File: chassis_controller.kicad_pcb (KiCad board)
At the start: 2 copper layers, 99.3 x 72.7 mm, 128 parts, among them J1 Screw_Terminal_01x02, J10 Conn_01x04_Pin, J11 Conn_02x03_Odd_Even, J12 Conn_01x04_Pin, J13 Conn_01x04_Pin, J14 Conn_01x04_Pin, J15 Conn_01x04_Pin, J16 Conn_01x04_Pin, J17 Conn_01x04_Pin, J18 Conn_01x03_Pin, J19 Conn_01x03_Pin, J2 Conn_01x04_Pin, J20 Conn_01x03_Pin, J21 Conn_01x04_Pin, J22 Conn_01x03_Pin, J23 Conn_01x03_Pin, J24 Conn_01x03_Pin, J25 Conn_01x03_Pin, J3 Conn_01x02_Pin, J4 Conn_01x02_Pin, J5 Conn_01x03_Pin, J6 Conn_01x03_Pin, J7 Conn_01x04_Pin, J8 Conn_01x04_Pin, J9 Conn_01x04_Pin, Q2 HSBA100P04, Q4 HSBA100P04, U1 AP64500SP-13, U2 AMS1117-3.3, U3 DSHP04TSGER, U4 STM32F407VGT6TR, U5 PCA9685PW,118, U6 PCA9685PW,118, U7 MPU-6050, U8 SN65HVD230DR, X1 X32258MOB4SI

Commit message: Add improvements to project
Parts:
- removed J11: Conn_02x03_Odd_Even, Connector_IDC:IDC-Header_2x03_P2.54mm_Vertical
- added C46: 1000uF, Capacitor_THT:CP_Radial_D10.0mm_P5.00mm, F.Cu at (153.0, 115.8)
- added C47: 1000uF, Capacitor_THT:CP_Radial_D10.0mm_P5.00mm, F.Cu at (164.0, 115.8)
- added J26: Conn_01x06_Pin, Connector_JST:JST_PH_B6B-PH-K_1x06_P2.00mm_Vertical, F.Cu at (128.8, 66.6)
- added Q1: NMOS, Package_TO_SOT_SMD:SOT-23, B.Cu at (155.7, 129.0)
- added R16: 47k, Resistor_SMD:R_0805_2012Metric, B.Cu at (154.7, 122.8)
- BUZZER1, D3, U3: moved to F.Cu
- R1, R11, R4, R7: moved to B.Cu
- R19: value 10 -> 10k
- moved JP1 30.5 mm to (135.9, 121.7)
- moved J25 30.5 mm to (131.8, 127.4)
- moved R35 30.5 mm to (133.5, 121.7)
- moved R34 21.9 mm to (140.7, 112.5)
- moved U8 21.9 mm to (142.4, 116.5)
- moved R18 17.9 mm to (159.4, 130.0), turned to 180 degrees
- moved R19 15.8 mm to (154.7, 126.0), turned to 0 degrees
- moved C38 15.1 mm to (127.7, 80.8)
- moved D1 15.0 mm to (172.6, 129.1)
- moved D4 15.0 mm to (170.4, 129.1)
- moved D5 15.0 mm to (168.0, 129.1)
- moved D6 15.0 mm to (165.6, 129.0)
- moved R1 15.0 mm to (172.6, 125.6)
- moved R11 15.0 mm to (165.8, 125.5)
- moved R4 15.0 mm to (170.4, 125.5)
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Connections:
- Q4 pad 4: Net-(Q4-G) -> Net-(Q1-D)
- R18 pad 2: Net-(Q4-G) -> Net-(Q1-D)
- R19 pad 1: /SERVO_PWR -> Net-(Q1-G)
- R19 pad 2: Net-(Q4-G) -> GND
- U4 pad 25: /MOTOR3_PWM -> unconnected-(U4-PA2-Pad25)
- U4 pad 26: /MOTOR4_PWM -> unconnected-(U4-PA3-Pad26)
- U4 pad 61: /MOTOR1_PWM -> unconnected-(U4-PD14-Pad61)
- U4 pad 62: /MOTOR2_PWM -> unconnected-(U4-PD15-Pad62)
- U5 pad 10: /MOTOR1_FWD -> /MOTOR1_PWM
- U5 pad 11: /MOTOR1_RVR -> /MOTOR1_FWD
- U5 pad 12: /MOTOR2_FWD -> /MOTOR1_RVR
- U5 pad 13: /MOTOR2_RVR -> /MOTOR2_PWM
- U5 pad 15: /MOTOR3_FWD -> /MOTOR2_FWD
- U5 pad 16: /MOTOR3_RVR -> /MOTOR2_RVR
- U5 pad 17: /MOTOR4_FWD -> /MOTOR3_PWM
- U5 pad 18: /MOTOR4_RVR -> /MOTOR3_FWD
- U5 pad 19: unconnected-(U5-LED12-Pad19) -> /MOTOR3_RVR
- U5 pad 20: unconnected-(U5-LED13-Pad20) -> /MOTOR4_PWM
- U5 pad 21: unconnected-(U5-LED14-Pad21) -> /MOTOR4_FWD
- U5 pad 22: unconnected-(U5-LED15-Pad22) -> /MOTOR4_RVR
- X1 pad 2: /OSC_IN -> GND
- X1 pad 3: GND -> /OSC_IN

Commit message: Update project
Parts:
- removed C39: 10nF, Capacitor_SMD:C_0805_2012Metric
- added C48: 1000uF, Capacitor_THT:CP_Radial_D10.0mm_P5.00mm, F.Cu at (150.0, 117.5)
- added G***: LOGO, kpi-rover:kpi-rover-logo, F.Cu at (121.3, 108.7)
- added Q3: NMOS, Package_TO_SOT_SMD:SOT-23, B.Cu at (169.6, 71.1)
- added R36: 4.7k, Resistor_SMD:R_0805_2012Metric, B.Cu at (173.6, 70.2)
- added R37: 4.7k, Resistor_SMD:R_0805_2012Metric, B.Cu at (182.6, 125.8)
- added R38: 0, Resistor_SMD:R_0805_2012Metric, B.Cu at (191.8, 70.3)
- added R39: 0, Resistor_SMD:R_0805_2012Metric, B.Cu at (182.6, 128.2)
- added R40: 0, Resistor_SMD:R_0805_2012Metric, B.Cu at (141.9, 118.4)
- added R41: 330, Resistor_SMD:R_0805_2012Metric, B.Cu at (173.6, 62.0)
- added R42: 1k, Resistor_SMD:R_0805_2012Metric, B.Cu at (155.7, 69.0)
- added R43: 1k, Resistor_SMD:R_0805_2012Metric, B.Cu at (141.0, 69.0)
- added R44: 2k, Resistor_SMD:R_0805_2012Metric, B.Cu at (155.7, 72.0)
- added R45: 2k, Resistor_SMD:R_0805_2012Metric, B.Cu at (141.0, 72.0)
- added R46: 0, Resistor_SMD:R_0805_2012Metric, B.Cu at (154.8, 75.7)
- added R47: 0, Resistor_SMD:R_0805_2012Metric, B.Cu at (123.1, 88.3)
- added R48: 0, Resistor_SMD:R_0805_2012Metric, B.Cu at (170.1, 130.5)
- added R49: 0, Resistor_SMD:R_0805_2012Metric, B.Cu at (127.9, 84.6)
- added R50: 0, Resistor_SMD:R_0805_2012Metric, B.Cu at (194.7, 65.0)
- added R51: 0, Resistor_SMD:R_0805_2012Metric, B.Cu at (170.4, 96.4)
- added R52: 0, Resistor_SMD:R_0805_2012Metric, B.Cu at (140.3, 87.0)
- C46: value 1000uF -> 100nF; footprint Capacitor_THT:CP_Radial_D10.0mm_P5.00mm -> Capacitor_SMD:C_0805_2012Metric; moved to B.Cu
- J3: value Conn_01x02_Pin -> Screw_Terminal_01x02; footprint Connector_JST:JST_PH_B2B-PH-K_1x02_P2.00mm_Vertical -> DB127V-5.08-2P-GN-S:CONN-TH_2P-P5.08
- moved C1 57.1 mm to (153.8, 79.2)
- moved C46 46.1 mm to (131.3, 75.2), turned to -90 degrees
- moved J22 16.4 mm to (192.4, 105.2), turned to -90 degrees
- moved J24 13.9 mm to (199.4, 105.2), turned to -90 degrees
- moved J26 13.8 mm to (115.2, 64.5), turned to 0 degrees
- moved C26 13.7 mm to (129.6, 65.4)
- moved C27 13.6 mm to (129.6, 67.6)
- moved D6 13.5 mm to (179.0, 130.4)
- moved C10 13.3 mm to (178.3, 87.4), turned to 90 degrees
- moved R11 13.2 mm to (179.0, 126.4)
- moved C12 13.2 mm to (185.3, 87.4), turned to 90 degrees
- moved C19 13.2 mm to (199.5, 87.4), turned to 90 degrees
- moved C17 13.1 mm to (192.4, 87.4), turned to 90 degrees
- moved C13 12.8 mm to (183.2, 87.4), turned to 90 degrees
- moved C11 12.8 mm to (176.2, 87.4), turned to 90 degrees
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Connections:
- BUZZER1 pad 1: +5V -> Net-(BUZZER1-Pad1)
- BUZZER1 pad 2: /BUZZER_OUT -> Net-(Q3-D)
- C15 pad 1: +5V -> Net-(U2-VIN)
- C36 pad 1: +5V -> Net-(U5-VDD)
- C37 pad 1: +5V -> Net-(U6-VDD)
- C43 pad 1: +3.3V -> Net-(U7-VDD)
- C46 pad 1: /SERVO_5V -> GND
- C46 pad 2: GND -> Net-(U7-VDD)
- C47 pad 1: /SERVO_5V -> +5V
- J14 pad 4: /USS1_ECHO -> Net-(J14-Pin_4)
- J15 pad 4: /USS2_ECHO -> Net-(J15-Pin_4)
- R1 pad 2: +5V -> Net-(R1-Pad2)
- R11 pad 2: +5V -> Net-(R1-Pad2)
- R22 pad 1: +3.3V -> Net-(R22-Pad1)
- R23 pad 1: +3.3V -> Net-(R22-Pad1)
- R24 pad 1: +3.3V -> Net-(R22-Pad1)
- R25 pad 1: +3.3V -> Net-(R22-Pad1)
- R28 pad 1: +5V -> Net-(R28-Pad1)
- R29 pad 1: +5V -> Net-(R28-Pad1)
- R30 pad 1: +3.3V -> Net-(U7-VDD)
- R31 pad 1: +3.3V -> Net-(U7-VDD)
- R4 pad 2: +5V -> Net-(R1-Pad2)
- R7 pad 2: +5V -> Net-(R1-Pad2)
- U2 pad 3: +5V -> Net-(U2-VIN)
- U5 pad 1: GND -> Net-(U5-A0)
- U5 pad 28: +5V -> Net-(U5-VDD)
- U6 pad 2: GND -> Net-(U6-A1)
- U6 pad 28: +5V -> Net-(U6-VDD)
- U7 pad 13: +3.3V -> Net-(U7-VDD)
- U7 pad 8: +3.3V -> Net-(U7-VDD)
- U7 pad 9: unconnected-(U7-AD0-Pad9) -> GND
- U8 pad 3: +3.3V -> Net-(U8-VCC)
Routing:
- net +3.3V: track 0.00 -> 302.1 mm, vias 0 -> 13
- net +5V: track 0.00 -> 241.8 mm, vias 0 -> 136
- net /SERVO_5V: track 0.00 -> 135.8 mm, vias 0 -> 18
- net /PCA_I2C_SCL: track 0.00 -> 103.3 mm, vias 0 -> 4
- net /PCA_I2C_SDA: track 0.00 -> 102.7 mm, vias 0 -> 4
- net /POWER_SUPPLY_ADC: track 0.00 -> 69.3 mm, vias 0 -> 2
- net /SWCLK: track 0.00 -> 53.3 mm, vias 0 -> 1
- net /ENC4_B: track 0.00 -> 52.7 mm, vias 0 -> 1
- net /ENC4_A: track 0.00 -> 52.7 mm, vias 0 -> 1
- net /SWDIO: track 0.00 -> 51.2 mm, vias 0 -> 1
- net /STATUS_LED_4: track 0.00 -> 47.1 mm, vias 0 -> 1
- net /ENC2_A: track 0.00 -> 44.4 mm, vias 0 -> 1
- net /ENC2_B: track 0.00 -> 44.2 mm, vias 0 -> 1
- net /NRST: track 0.00 -> 44.2 mm
- net /STATUS_LED_3: track 0.00 -> 43.9 mm, vias 0 -> 1
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- added copper zone on B.Cu, net +3.3V
- added copper zone on B.Cu, net +5V
- added copper zone on F.Cu, net +5V
- added copper zone on B.Cu, net /USS1_ECHO
- added copper zone on B.Cu, net /USS2_ECHO
- added copper zone on B.Cu, net GND
- added copper zone on F.Cu, net GND
- added copper zone on B.Cu, net Net-(U1-EN)
- added copper zone on B.Cu, net VCC
- added copper zone on F.Cu, net VCC
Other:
- board size 99.3 x 72.7 mm -> 100 x 75 mm
- board text added: "A"
- board text added: "B"
- board text added: "CANH"
- board text added: "CANL"
- board text added: "ECHO"
- board text added: "F"
- board text added: "G"
- board text added: "GND"
- board text added: "KPI Rover Chassis Controller (ECU)"
- board text added: "NRST"
- board text added: "PWM"
- board text added: "R"
- board text added: "RX"
- board text added: "S/N:"
- board text added: "SCL"
- board text added: "SDA"
- board text added: "SWCLK"
- board text added: "SWDIO"
- board text added: "SWO"
- board text added: "TRIG"
- board text added: "TX"
- board text added: "Y"

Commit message: Update project
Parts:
- moved C7 16.1 mm to (132.3, 110.5)
- moved C9 13.7 mm to (118.7, 111.1), turned to 0 degrees
- moved R15 13.0 mm to (118.6, 113.2), turned to 180 degrees
- moved C3 12.0 mm to (119.9, 117.2), turned to 90 degrees
- moved C2 11.6 mm to (128.8, 108.5), turned to 0 degrees
- moved R10 8.96 mm to (122.1, 117.1), turned to 90 degrees
- moved R14 8.45 mm to (128.5, 116.2), turned to 180 degrees
- moved C8 7.64 mm to (121.5, 112.2), turned to 90 degrees
- moved R12 5.06 mm to (124.9, 116.2), turned to 0 degrees
- moved U1 3.95 mm to (126.7, 112.6), turned to -90 degrees
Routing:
- net Net-(U1-EN): track 5.99 -> 29.9 mm, vias 0 -> 2
- net +5V: track 241.8 -> 251.6 mm, vias 136 -> 137
- net Net-(U1-SW): track 19.1 -> 15.8 mm, vias 2 -> 0
- net Net-(U1-BST): track 3.00 -> 2.16 mm

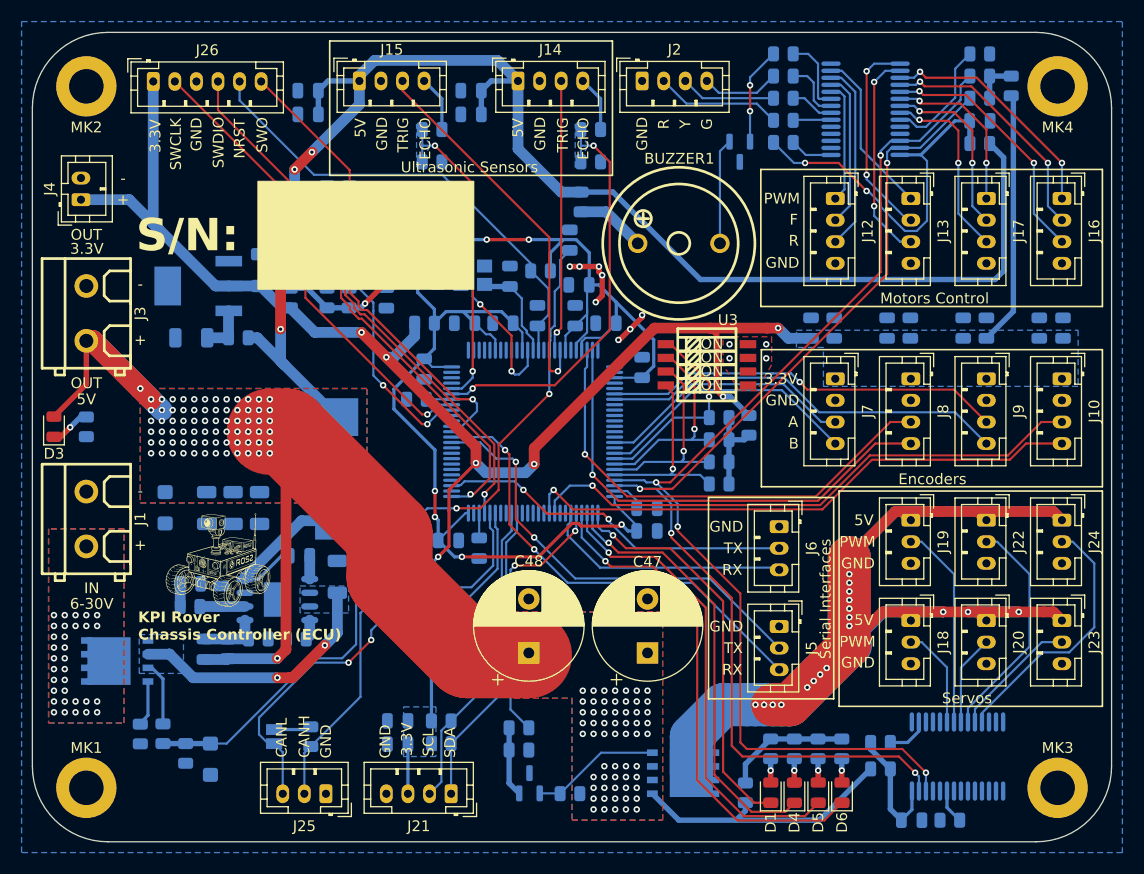
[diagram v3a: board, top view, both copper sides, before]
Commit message: Issue #4: Improve DC-DC layout. Prepare for production.
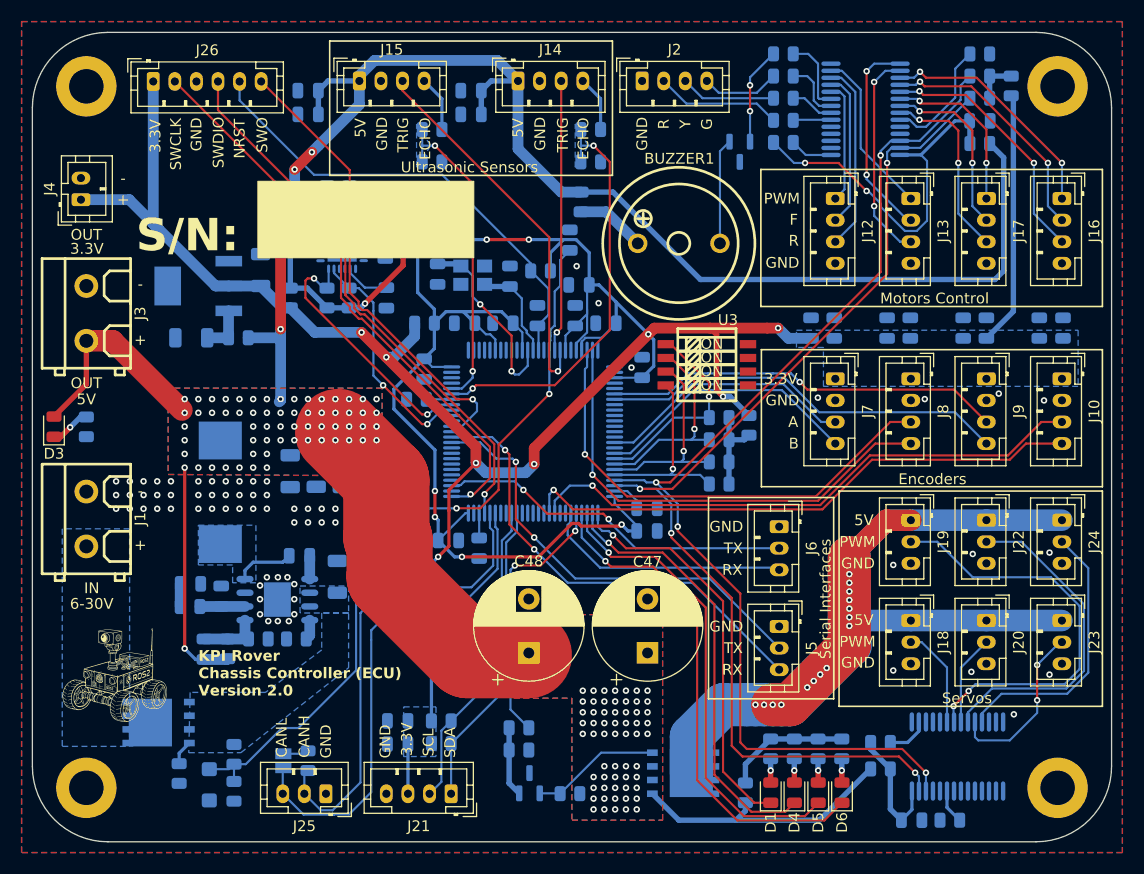
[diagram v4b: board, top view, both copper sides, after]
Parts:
- MK1: moved to B.Cu
- moved D7 19.2 mm to (135.3, 100.7)
- moved G*** 14.3 mm to (111.7, 119.4)
- moved C6 13.0 mm to (132.7, 100.7)
- moved L1 11.0 mm to (121.4, 102.6)
- moved C5 8.44 mm to (130.3, 100.6)
- moved Q2 6.87 mm to (115.7, 124.0)
- moved R6 6.85 mm to (122.7, 126.9)
- moved R2 5.69 mm to (122.7, 130.3)
- moved R13 5.14 mm to (117.6, 128.7)
- moved C4 4.44 mm to (127.9, 100.7)
- moved JP1 2.40 mm to (127.3, 127.5)
- moved D2 2.37 mm to (120.4, 129.7)
- moved R35 2.24 mm to (129.5, 127.5)
- turned MK1 to 0 degrees
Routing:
- net /SERVO_5V: track 135.8 -> 95.4 mm, vias 18 -> 15
- net Net-(U1-EN): track 29.9 -> 0.00 mm, vias 2 -> 0
- net +5V: track 251.6 -> 231.2 mm, vias 137 -> 126
- net /SERVO2_PWM: track 18.9 -> 38.5 mm, vias 0 -> 2
- net Net-(U1-SW): track 15.8 -> 5.46 mm
- net GND: track 9.64 -> 0.00 mm, vias 12 -> 67
- net /SERVO4_PWM: track 21.3 -> 30.8 mm
- net Net-(J25-Pin_2): track 22.4 -> 28.4 mm
- net Net-(J25-Pin_3): track 25.2 -> 29.9 mm, vias 2 -> 0
- net /SERVO5_PWM: track 11.8 -> 16.0 mm, vias 0 -> 2
- net Net-(Q2-G): track 4.24 -> 2.30 mm
- net Net-(JP1-A): track 3.50 -> 2.40 mm
- net /SERVO6_PWM: track 24.3 -> 25.4 mm
- net +3.3V: vias 13 -> 14
- net VCC: vias 32 -> 0
- added copper zone on B.Cu, net Net-(U1-SW)
- removed copper zone on F.Cu, net VCC
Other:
- board text added: "KPI Rover Chassis Controller (ECU) Version 2.0"
- board text removed: "KPI Rover Chassis Controller (ECU)"
